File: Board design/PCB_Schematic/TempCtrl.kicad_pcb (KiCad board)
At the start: 4 copper layers, 80 x 100 mm, 162 parts, among them CON1 BARREL_JACK, IC1 ATMEGA328P-A, P1 233-2977, P2 820-8104, P3 RS485, P4 USB_OTG, P5 ICSP, P6 ADC breakout, SW1 DISABLE_COMMS, U1 LM7805, U10 INA330, U11 ISO7242, U12 FT232RL, U13 ADS1262, U14 AD8639, U15 DAC8564, U16 AD8639, U17 DAC8564, U2 TMA0505S, U3 ADuM7642CRQZ, U4 ISO3088, U5 OPA548, U6 OPA548, U7 OPA548, U8 OPA548, U9 INA330, X1 TSX-3225 X1E0000210013

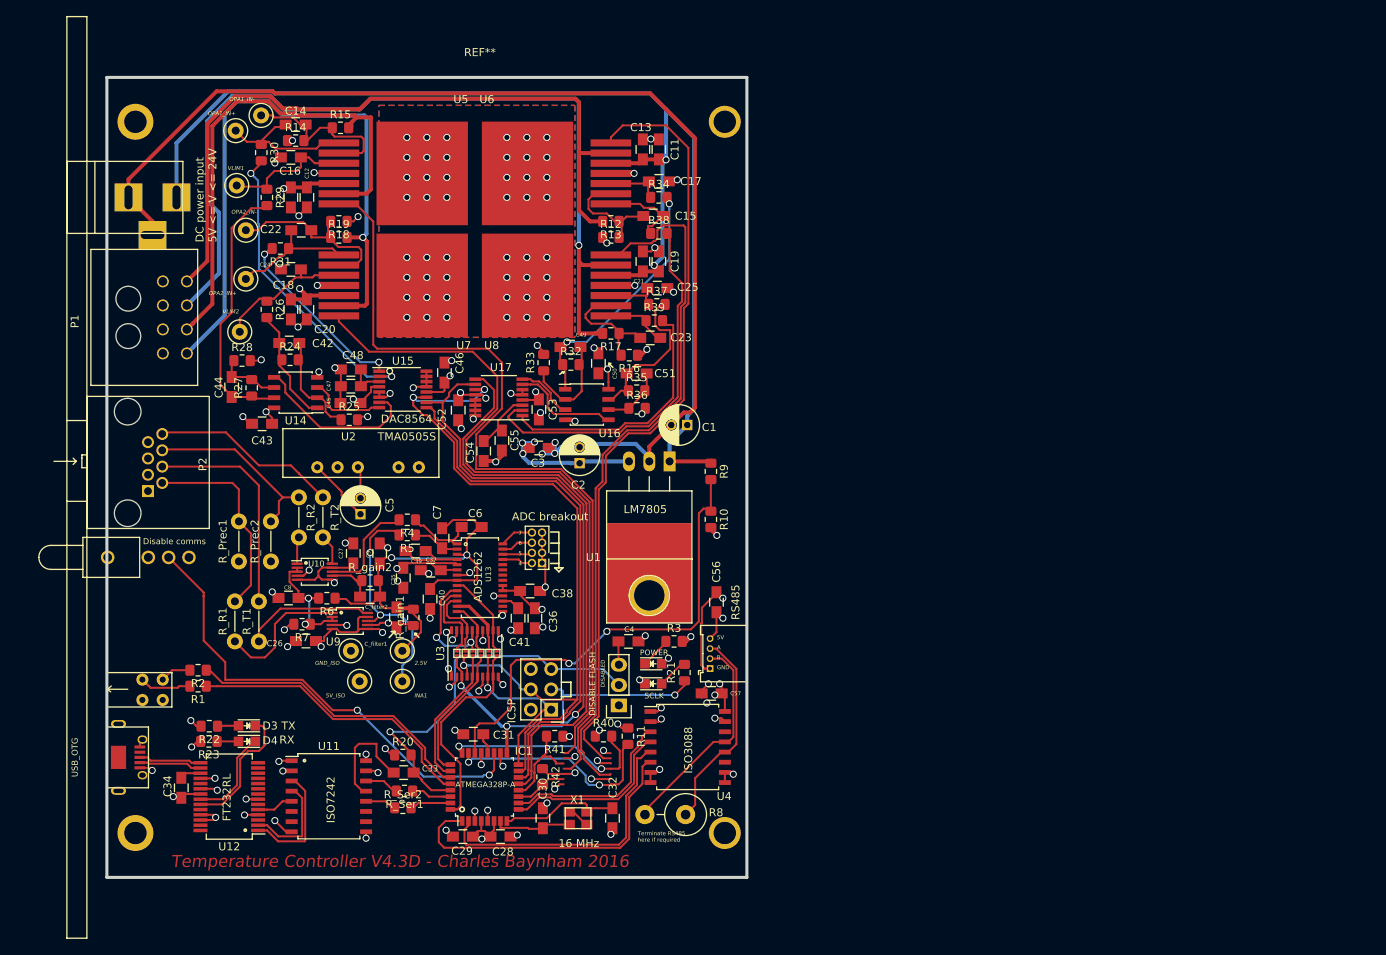
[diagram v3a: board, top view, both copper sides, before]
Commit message: PCB: buffer, ext ref, OPA jumpers, MMCX conn
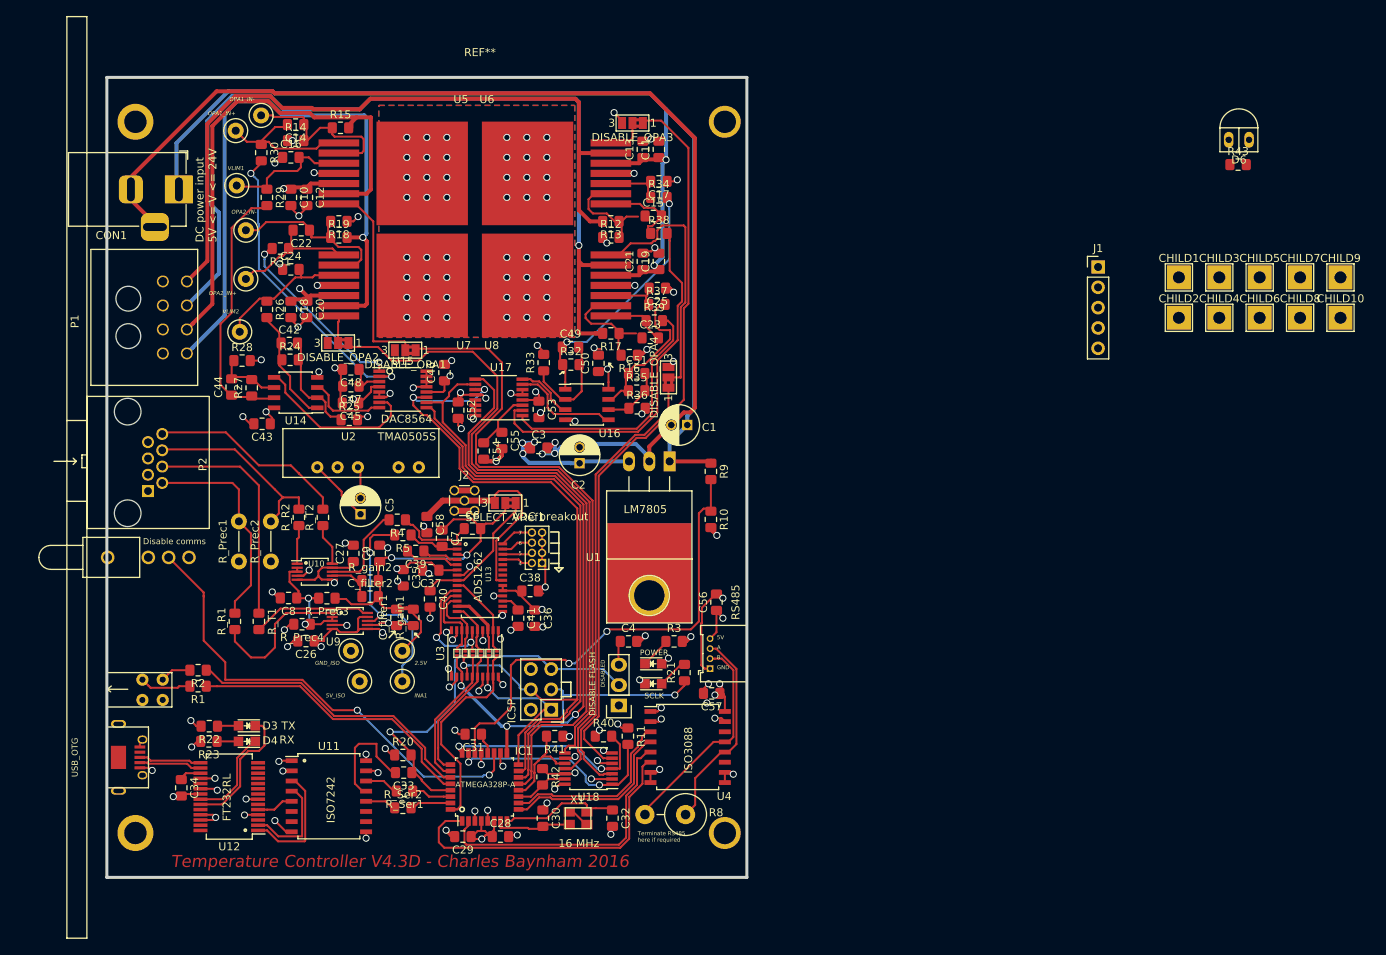
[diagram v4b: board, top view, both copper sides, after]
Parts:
- added C58: 100n, Capacitor_SMD:C_0805_2012Metric_Pad1.15x1.40mm_HandSolder, F.Cu at (205.0, 90.9)
- added CHILD1: PIN, TestPoint:TestPoint_THTPad_3.0x3.0mm_Drill1.5mm, F.Cu at (299.0, 60.0)
- added CHILD10: PIN, TestPoint:TestPoint_THTPad_3.0x3.0mm_Drill1.5mm, F.Cu at (319.2, 65.0)
- added CHILD2: PIN, TestPoint:TestPoint_THTPad_3.0x3.0mm_Drill1.5mm, F.Cu at (299.0, 65.0)
- added CHILD3: PIN, TestPoint:TestPoint_THTPad_3.0x3.0mm_Drill1.5mm, F.Cu at (304.1, 60.0)
- added CHILD4: PIN, TestPoint:TestPoint_THTPad_3.0x3.0mm_Drill1.5mm, F.Cu at (304.1, 65.0)
- added CHILD5: PIN, TestPoint:TestPoint_THTPad_3.0x3.0mm_Drill1.5mm, F.Cu at (309.1, 60.0)
- added CHILD6: PIN, TestPoint:TestPoint_THTPad_3.0x3.0mm_Drill1.5mm, F.Cu at (309.1, 65.0)
- added CHILD7: PIN, TestPoint:TestPoint_THTPad_3.0x3.0mm_Drill1.5mm, F.Cu at (314.1, 60.0)
- added CHILD8: PIN, TestPoint:TestPoint_THTPad_3.0x3.0mm_Drill1.5mm, F.Cu at (314.1, 65.0)
- added CHILD9: PIN, TestPoint:TestPoint_THTPad_3.0x3.0mm_Drill1.5mm, F.Cu at (319.2, 60.0)
- added D6: LED, Custom:PCB_MOUNT_LED, F.Cu at (306.5, 42.8)
- added DISABLE_OPA1: Disable_OPA1, Jumper:SolderJumper-3_P1.3mm_Bridged2Bar12_Pad1.0x1.5mm_NumberLabels, F.Cu at (202.3, 69.1)
- added DISABLE_OPA2: Disable_OPA2, Jumper:SolderJumper-3_P1.3mm_Bridged2Bar12_Pad1.0x1.5mm_NumberLabels, F.Cu at (193.9, 68.2)
- added DISABLE_OPA3: Disable_OPA3, Jumper:SolderJumper-3_P1.3mm_Bridged2Bar12_Pad1.0x1.5mm_NumberLabels, F.Cu at (230.7, 40.7)
- added DISABLE_OPA4: Disable_OPA4, Jumper:SolderJumper-3_P1.3mm_Bridged2Bar12_Pad1.0x1.5mm_NumberLabels, F.Cu at (235.2, 72.5)
- added J1: 5V_Outputs, Connector_PinHeader_2.54mm:PinHeader_1x05_P2.54mm_Vertical, F.Cu at (288.9, 58.7)
- added J2: External ref, Connector_Coaxial:MMCX_Molex_73415-1471_Vertical, F.Cu at (209.7, 87.9)
- added R43: 100R, Resistor_SMD:R_0805_2012Metric_Pad1.15x1.40mm_HandSolder, F.Cu at (306.4, 45.9)
- added SELECT_VRef1: Select V_ref, Jumper:SolderJumper-3_P1.3mm_Bridged2Bar12_Pad1.0x1.5mm_NumberLabels, F.Cu at (214.8, 88.2)
- added U18: 74LS125, Package_SO:TSSOP-14_4.4x5mm_P0.65mm, F.Cu at (225.2, 121.4)
- C10, C11, C12, C13, C14, C15, C16, C17, C18, C19, C20, C21, C22, C23, C24, C25, C26, C27, C28, C29, C3, C30, C31, C32, C33, C34, C35, C36, C37, C38, C39, C4, C40, C41, C42, C43, C44, C45, C46, C47, C48, C49, C50, C51, C52, C53, C54, C55, C56, C57, C6, C7, C8, C9, C_filter1, C_filter2: footprint Capacitors_SMD:C_0805_HandSoldering -> Capacitor_SMD:C_0805_2012Metric_Pad1.15x1.40mm_HandSolder
- CON1: footprint Connect:BARREL_JACK -> Connector_BarrelJack:BarrelJack_Horizontal
- R11, R40, R41, R42: value R_Small -> 10k
- R_Prec1, R_Prec2: value R -> 10k_prec
- R_Prec3: renamed from R6; value 15k -> 33k_prec
- R_Prec4: renamed from R7; value 10k -> 22k_prec
- R_R1, R_R2, R_T1, R_T2: value R_series -> 1k_prec; footprint Custom:Resistor_Vertical_RM5mm_Cust -> Resistor_SMD:R_0805_2012Metric_Pad1.15x1.40mm_HandSolder
- R_gain1, R_gain2: value 24K -> 22k_prec
- moved CON1 6.58 mm to (174.0, 49.0)
- moved R4 1.25 mm to (201.3, 90.3)
- moved R5 0.55 mm to (202.0, 92.2)
- moved C6 0.22 mm to (210.7, 91.4)
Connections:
- C6 pad 2: /ADC_2.5_REF -> /INA_2.5V_REF
- C7 pad 1: /ADC_2.5_REF -> /INA_2.5V_REF
- C9 pad 1: /ADC_2.5_REF -> /INA_2.5V_REF
- C_filter1 pad 2: /ADC_2.5_REF -> /INA_2.5V_REF
- C_filter2 pad 2: /ADC_2.5_REF -> /INA_2.5V_REF
- R_Prec3 pad 1: /ADC_2.5_REF -> /INA_2.5V_REF
- R_gain1 pad 2: /ADC_2.5_REF -> /INA_2.5V_REF
- R_gain2 pad 2: /ADC_2.5_REF -> /INA_2.5V_REF
- U13 pad 21: /ADC_Chip/ADC_IN0 -> /EXT_REF_P
- U13 pad 22: /ADC_Chip/ADC_IN1 -> /ANALOG_GND
- U13 pad 3: /ADC_2.5_REF -> /INA_2.5V_REF
- U5 pad 7: /ES1_OUT -> Net-(DISABLE_OPA1-Pad2)
- U6 pad 7: /ES3_OUT -> Net-(DISABLE_OPA3-Pad2)
- U7 pad 7: /ES2_OUT -> Net-(DISABLE_OPA2-Pad2)
- U8 pad 7: /ES4_OUT -> Net-(DISABLE_OPA4-Pad2)
- W3 pad 1: /ADC_2.5_REF -> /INA_2.5V_REF
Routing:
- net /INA_2.5V_REF: track 0.00 -> 51.8 mm, vias 0 -> 2
- net /ADC_2.5_REF: track 56.6 -> 17.1 mm, vias 2 -> 0
- net /ES4_OUT: track 93.2 -> 56.3 mm
- net Net-(DISABLE_OPA4-Pad2): track 0.00 -> 36.0 mm
- net /EXT_REF_P: track 0.00 -> 27.0 mm
- net /ES1_OUT: track 104.3 -> 77.9 mm
- net Net-(DISABLE_OPA1-Pad2): track 0.00 -> 25.2 mm
- net /ANALOG_GND: track 34.8 -> 41.7 mm, vias 18 -> 19
- net /ES3_OUT: track 97.4 -> 91.7 mm
- net Net-(DISABLE_OPA3-Pad2): track 0.00 -> 4.84 mm
- net Net-(DISABLE_OPA2-Pad2): track 0.00 -> 3.43 mm
- net /ES2_OUT: track 86.3 -> 83.8 mm
- net Earth_Clean: track 248.7 -> 251.0 mm, vias 110 -> 112
- net /ADC_Chip/ADC_IN8: track 8.97 -> 10.8 mm
- net /INA2_T: track 23.5 -> 25.0 mm
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
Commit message: Replace VCC routes with fill on internal layer, where 5V isn't needed
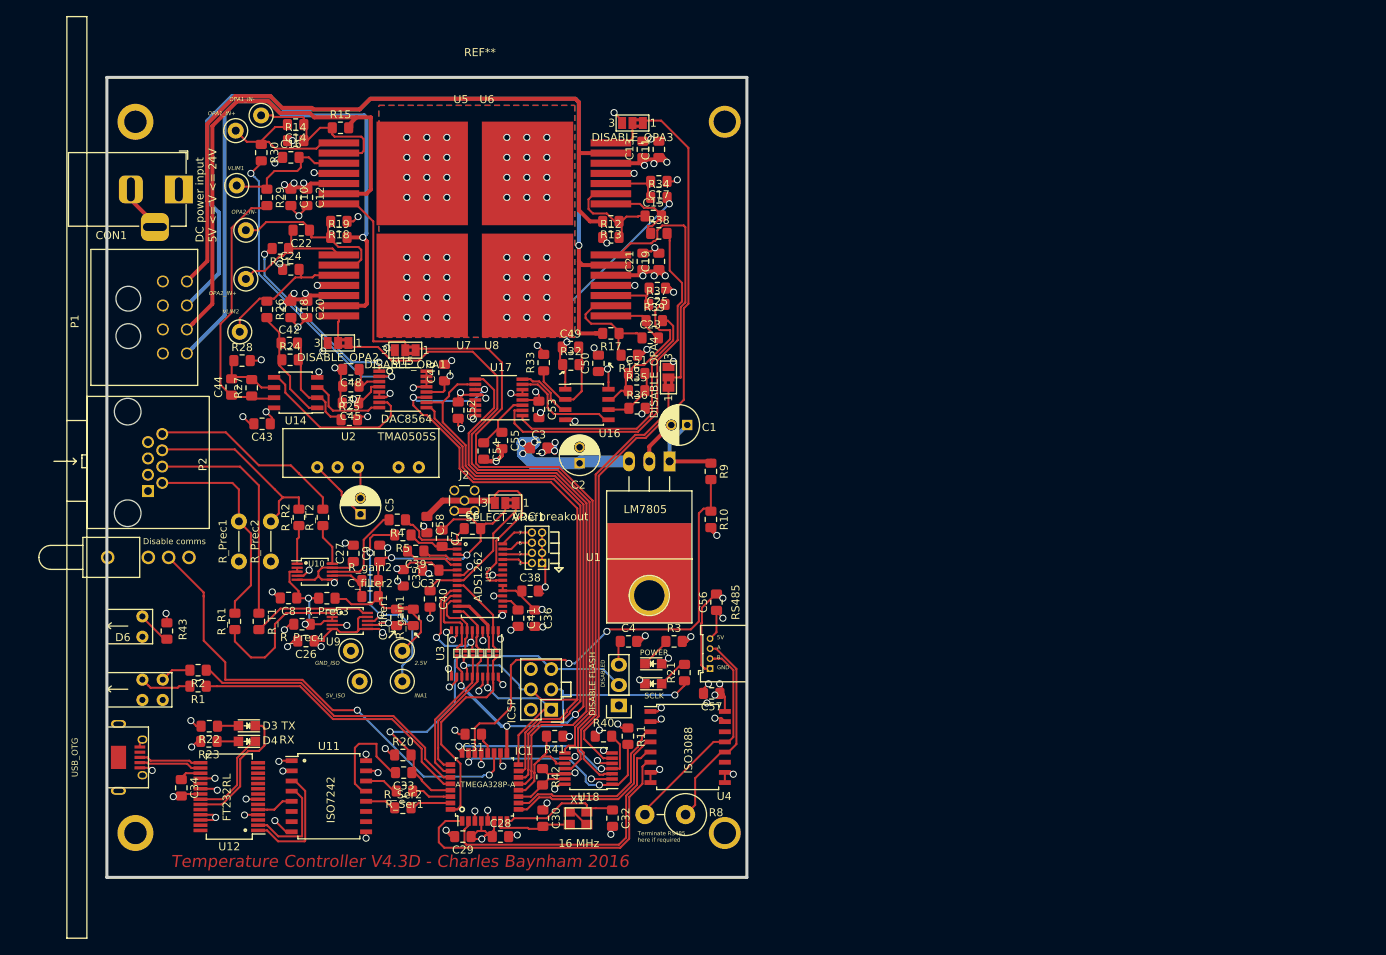
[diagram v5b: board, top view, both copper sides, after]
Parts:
- removed CHILD1, CHILD10, CHILD2, CHILD3, CHILD4, CHILD5, CHILD6, CHILD7, CHILD8, CHILD9: PIN, TestPoint:TestPoint_THTPad_3.0x3.0mm_Drill1.5mm
- removed J1: 5V_Outputs, Connector_PinHeader_2.54mm:PinHeader_1x05_P2.54mm_Vertical
- moved D6 153.2 mm to (165.0, 101.5)
- moved R43 146.0 mm to (172.5, 104.2), turned to 90 degrees
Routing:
- net VCC: track 198.0 -> 48.3 mm, vias 4 -> 12
- net Earth_Clean: track 251.0 -> 125.0 mm, vias 112 -> 114
- net Net-(D6-Pad2): track 0.00 -> 4.09 mm
- net +5V: track 62.7 -> 65.8 mm, vias 19 -> 20
- net /EXT_REF_P: track 27.0 -> 28.5 mm
- net Net-(C49-Pad1): track 31.0 -> 29.6 mm
- net /ANALOG_GND: track 41.7 -> 40.5 mm, vias 19 -> 20
- net /OPA4_IN-: track 16.3 -> 17.3 mm
- net /OPA3_IN-: track 13.4 -> 14.3 mm
- net /DACOutputs1/DAC_OUT_D: track 22.9 -> 23.5 mm
- added copper zone on In2.Cu, net VCC

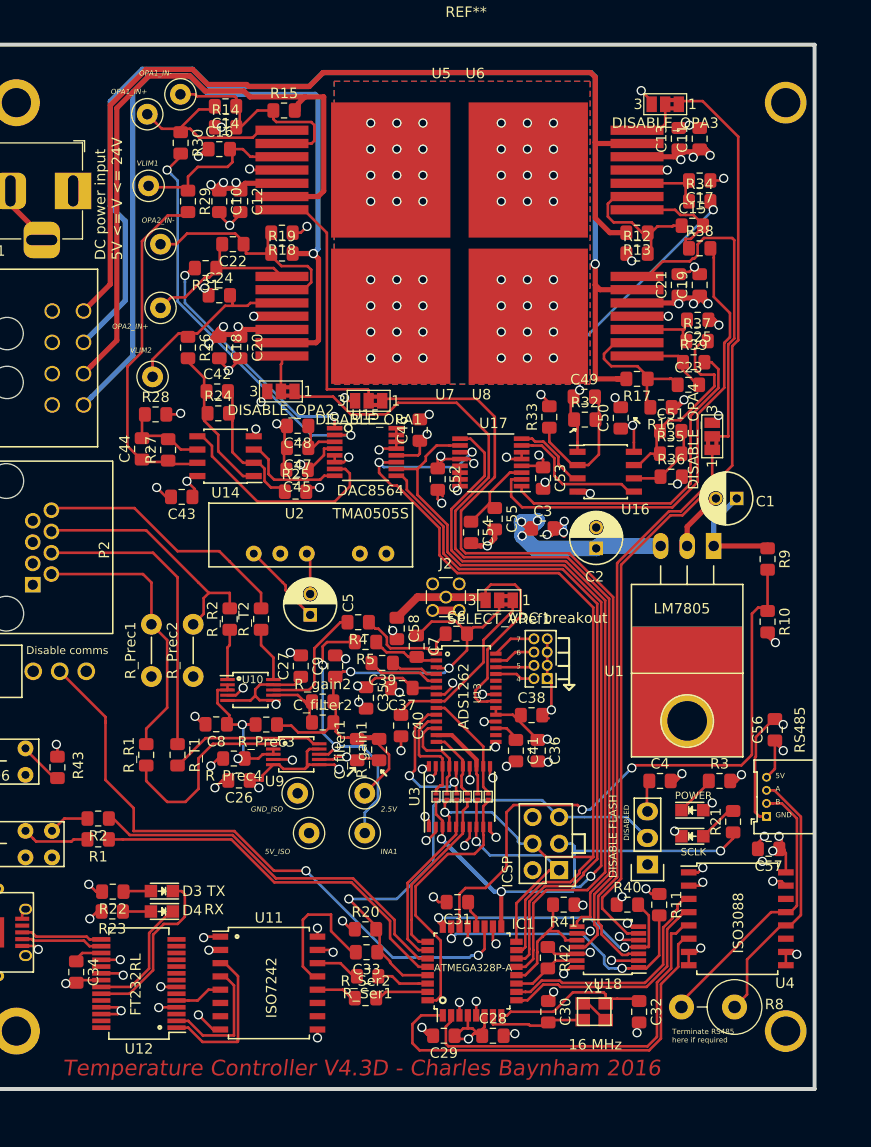
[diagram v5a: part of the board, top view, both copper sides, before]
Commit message: PCB: Connections for daughterboard
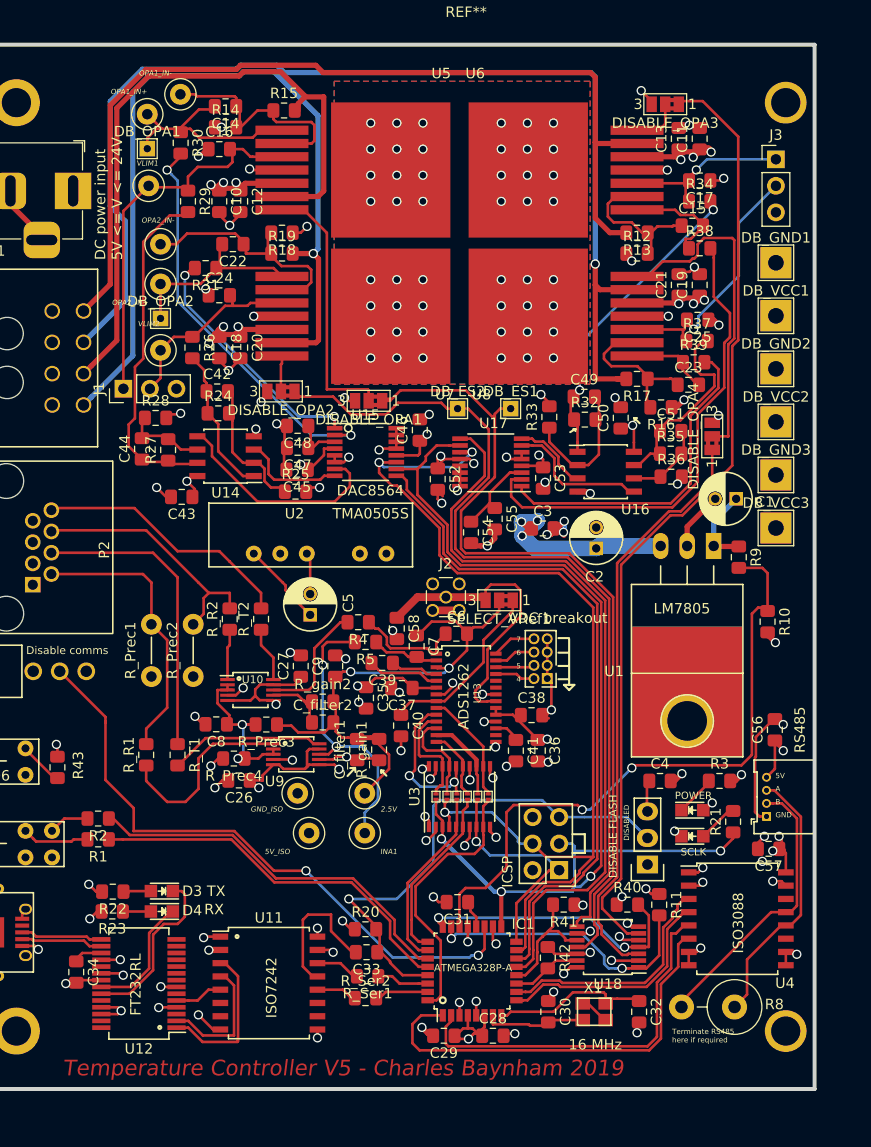
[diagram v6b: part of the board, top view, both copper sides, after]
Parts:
- added DB_ES1: PIN, TestPoint:TestPoint_THTPad_1.5x1.5mm_Drill0.7mm, F.Cu at (215.9, 69.8)
- added DB_ES2: PIN, TestPoint:TestPoint_THTPad_1.5x1.5mm_Drill0.7mm, F.Cu at (210.8, 69.8)
- added DB_GND1: PIN, TestPoint:TestPoint_THTPad_3.0x3.0mm_Drill1.5mm, F.Cu at (241.3, 55.9)
- added DB_GND2: PIN, TestPoint:TestPoint_THTPad_3.0x3.0mm_Drill1.5mm, F.Cu at (241.3, 66.0)
- added DB_GND3: PIN, TestPoint:TestPoint_THTPad_3.0x3.0mm_Drill1.5mm, F.Cu at (241.3, 76.2)
- added DB_OPA1: PIN, TestPoint:TestPoint_THTPad_1.5x1.5mm_Drill0.7mm, F.Cu at (181.1, 45.0)
- added DB_OPA2: PIN, TestPoint:TestPoint_THTPad_1.5x1.5mm_Drill0.7mm, F.Cu at (182.4, 61.2)
- added DB_VCC1: PIN, TestPoint:TestPoint_THTPad_3.0x3.0mm_Drill1.5mm, F.Cu at (241.3, 61.0)
- added DB_VCC2: PIN, TestPoint:TestPoint_THTPad_3.0x3.0mm_Drill1.5mm, F.Cu at (241.3, 71.1)
- added DB_VCC3: PIN, TestPoint:TestPoint_THTPad_3.0x3.0mm_Drill1.5mm, F.Cu at (241.3, 81.3)
- added J1: 5V_Outputs_1, Connector_PinHeader_2.54mm:PinHeader_1x03_P2.54mm_Vertical, F.Cu at (178.8, 67.9)
- added J3: 5V_Outputs_2, Connector_PinHeader_2.54mm:PinHeader_1x03_P2.54mm_Vertical, F.Cu at (241.3, 46.0)
- moved R9 2.76 mm to (237.7, 84.1)
- moved W10 2.65 mm to (182.4, 64.3)
- moved W8 2.29 mm to (182.4, 57.9)
- moved R26 0.42 mm to (185.4, 64.0)
- moved R28 0.34 mm to (181.9, 70.7)
- moved C1 0.07 mm to (237.5, 78.5)
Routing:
- net /VLIM1: track 16.1 -> 36.5 mm
- net /VLIM4: track 6.60 -> 24.7 mm, vias 0 -> 1
- net /VLIM3: track 6.90 -> 16.2 mm, vias 0 -> 1
- net /ES1_OUT: track 77.9 -> 81.5 mm
- net VCC: track 48.3 -> 45.0 mm
- net /DIYino/A7_inputonly: track 58.6 -> 61.6 mm
- net /OPA1_IN+: track 20.0 -> 22.7 mm
- net /OPA2_IN+: track 16.7 -> 18.9 mm
- net /VLIM2: track 17.4 -> 18.6 mm
- net /C4+_OUT: track 110.9 -> 110.1 mm
- net /C3+_OUT: track 90.8 -> 90.0 mm
- net /C2+_OUT: track 80.1 -> 79.3 mm
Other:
- board text added: "Temperature Controller V5 - Charles Baynham 2019"
- board text removed: "Temperature Controller V4.3D - Charles Baynham 2016"
